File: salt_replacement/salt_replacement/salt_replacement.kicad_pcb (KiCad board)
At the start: 2 copper layers, 35 x 21 mm, 17 parts, among them J1 SALT chip package pins, Q1 FDG1024NZ, U1 IC REG BUCK SEPIC 5V 4.5A 8SO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, U2 MAX3232

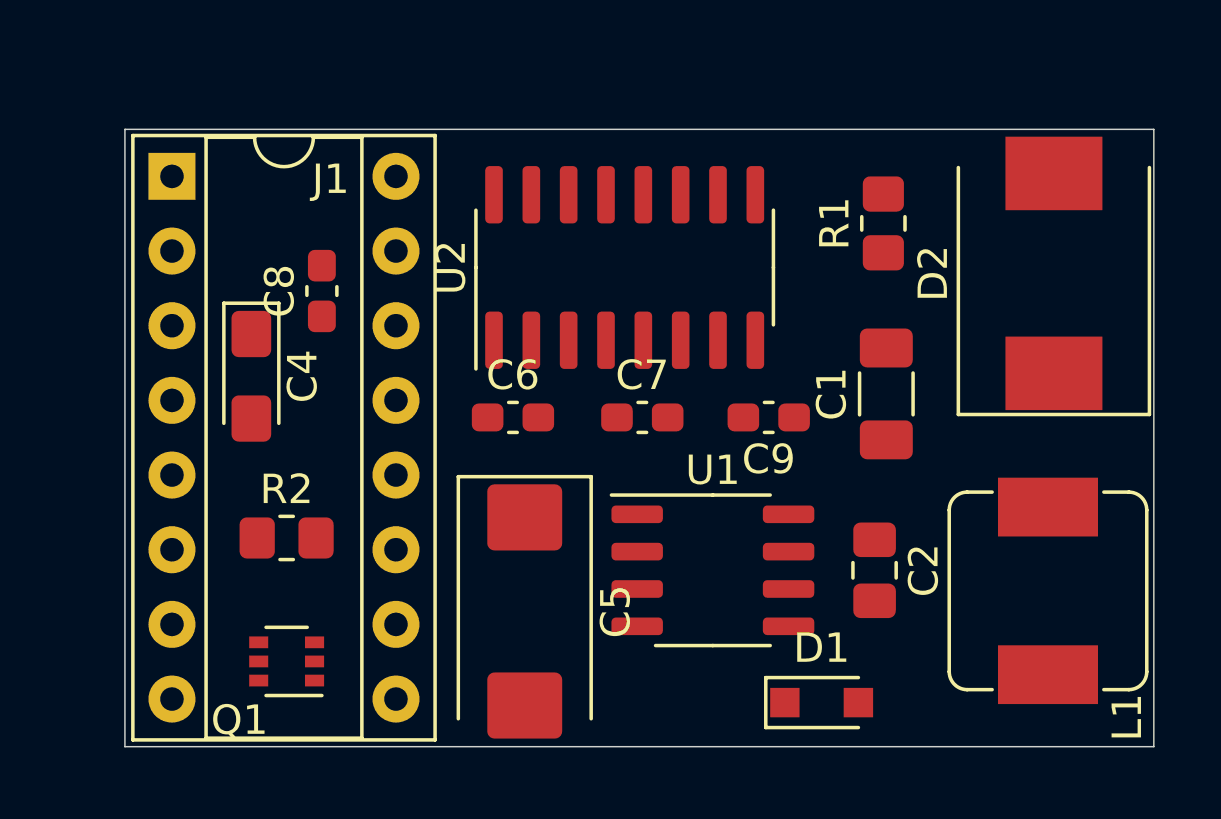
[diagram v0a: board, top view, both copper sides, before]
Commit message: -complete redesign -replaced all components with jclpcb stock -added non-inverting zero crossing circuit.
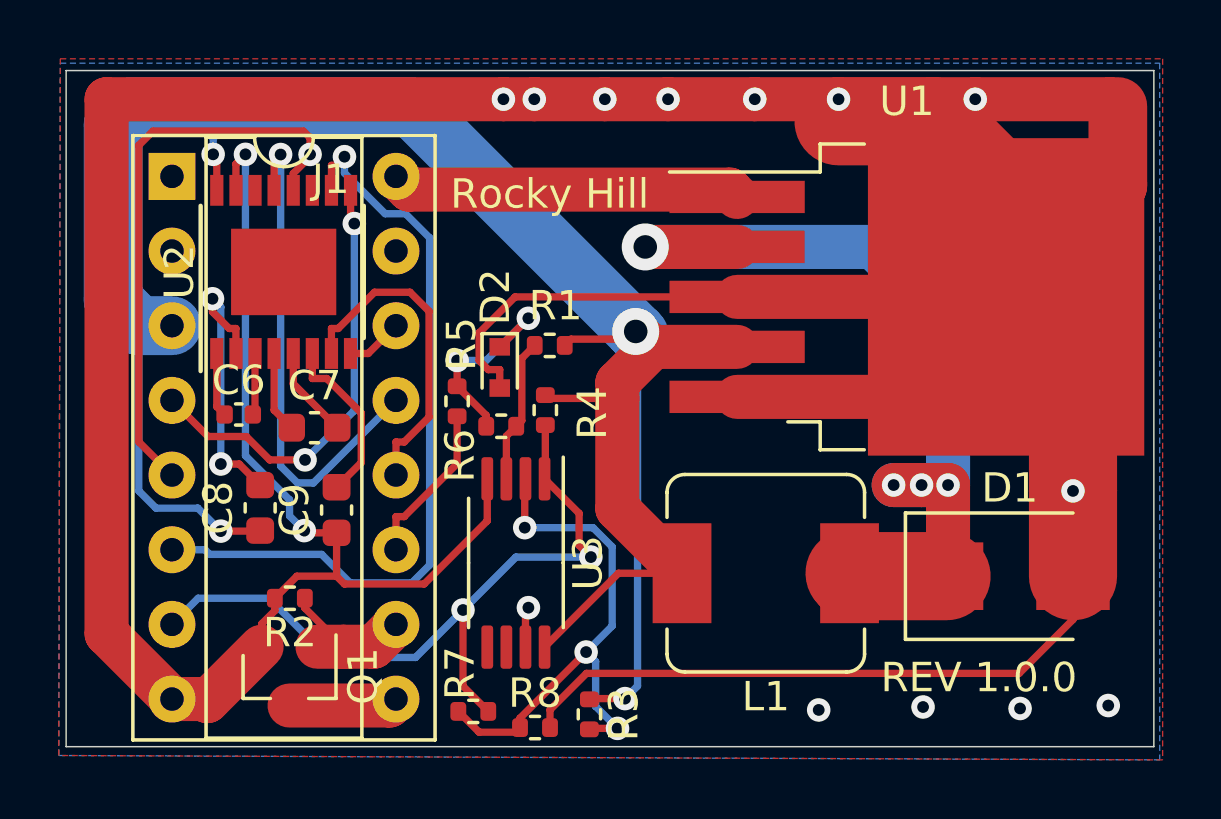
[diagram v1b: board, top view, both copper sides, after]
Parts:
- removed C1: .27uF, Capacitor_SMD:C_1206_3216Metric_Pad1.33x1.80mm_HandSolder
- removed C2: 5000pF, Capacitor_SMD:C_0805_2012Metric_Pad1.18x1.45mm_HandSolder
- removed C4: 10uF, Capacitor_Tantalum_SMD:CP_EIA-3216-18_Kemet-A_Pad1.58x1.35mm_HandSolder
- removed C5: 100uF, Capacitor_Tantalum_SMD:CP_EIA-7343-31_Kemet-D_Pad2.25x2.55mm_HandSolder
- added R3: 100K, Resistor_SMD:R_0402_1005Metric, F.Cu at (125.8, 129.9)
- added R4: 5.1K, Resistor_SMD:R_0402_1005Metric, F.Cu at (124.3, 119.5)
- added R5: 5.1K, Resistor_SMD:R_0402_1005Metric, F.Cu at (121.3, 119.2)
- added R6: 5.1K, Resistor_SMD:R_0402_1005Metric, F.Cu at (122.8, 120.1)
- added R7: 20M, Resistor_SMD:R_0402_1005Metric, F.Cu at (121.8, 129.8)
- added R8: 10K, Resistor_SMD:R_0402_1005Metric, F.Cu at (124.0, 130.3)
- added U3: LM393, Package_SO:TSSOP-8_4.4x3mm_P0.65mm, F.Cu at (123.3, 124.8)
- C6: footprint Capacitor_SMD:C_0603_1608Metric_Pad1.08x0.95mm_HandSolder -> Capacitor_SMD:C_0402_1005Metric
- C7, C8, C9: footprint Capacitor_SMD:C_0603_1608Metric_Pad1.08x0.95mm_HandSolder -> Capacitor_SMD:C_0603_1608Metric
- D1: value CMDSH-3 -> 5A 40V; footprint Diode_SMD:D_SOD-323_HandSoldering -> Diode_SMD:D_SMB
- D2: value B340LB-13-F -> 1N4148; footprint Diode_SMD:D_SMC -> Diode_SMD:D_SOD-523
- L1: value 10uH -> 33uH; footprint salt_replacement:L_Sumida_CDMC6D28_7.25x6.5mm -> Inductor_SMD:L_Sumida_CDMC6D28_7.25x6.5mm
- Q1: value FDG1024NZ -> MMBT9014C; footprint Package_TO_SOT_SMD:SOT-363_SC-70-6 -> Package_TO_SOT_SMD:SOT-23
- R1: value 10K -> 100K; footprint Resistor_SMD:R_0805_2012Metric_Pad1.20x1.40mm_HandSolder -> Resistor_SMD:R_0402_1005Metric
- R2: footprint Resistor_SMD:R_0805_2012Metric_Pad1.20x1.40mm_HandSolder -> Resistor_SMD:R_0402_1005Metric
- U1: value IC REG BUCK SEPIC 5V 4.5A 8SOIC -> LM2596S-5; footprint Package_SO:SO-8_3.9x4.9mm_P1.27mm -> Package_TO_SOT_SMD:TO-263-5_TabPin3
- U2: footprint Package_SO:SOIC-16_3.9x9.9mm_P1.27mm -> Package_SO:TSSOP-16-1EP_4.4x5mm_P0.65mm
- moved D2 19.1 mm to (122.8, 118.1), turned to 270 degrees
- moved C9 15.0 mm to (117.2, 123.0), turned to 90 degrees
- moved R1 12.1 mm to (124.5, 117.3), turned to 180 degrees
- moved U2 11.6 mm to (115.4, 114.8)
- moved U1 11.4 mm to (136.6, 115.7)
- moved C7 11.2 mm to (116.5, 120.2)
- moved L1 9.62 mm to (131.8, 125.1), turned to 180 degrees
- moved C6 9.33 mm to (113.9, 119.7)
- moved D1 7.71 mm to (140.1, 125.2)
- moved C8 7.67 mm to (114.6, 122.9)
- moved R2 2.05 mm to (115.6, 126.0), turned to 180 degrees
- moved Q1 0.51 mm to (115.6, 128.6), turned to 270 degrees
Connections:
- C8 pad 1: Net-(C8-Pad1) -> +5V
- C8 pad 2: +5V -> Net-(C8-Pad2)
- D1 pad 1: Net-(C1-Pad1) -> Net-(D1-Pad1)
- D1 pad 2: +5V -> GND
- D2 pad 1: Net-(C1-Pad2) -> Net-(D2-Pad1)
- J1 pad 11: Net-(J1-Pad11) -> /CASSETTE_DATA_IN
- J1 pad 7: Net-(J1-Pad7) -> /CASSETTE_DATA_IN_TTL
- L1 pad 1: Net-(C1-Pad2) -> Net-(D1-Pad1)
- Q1 pad 1: GND -> Net-(J1-Pad10)
- Q1 pad 2: Net-(J1-Pad10) -> GND
- Q1 pad 3: Net-(Q1-Pad3) -> Net-(J1-Pad9)
- R1 pad 1: Net-(C2-Pad1) -> +5V
- R1 pad 2: GND -> Net-(R1-Pad2)
- U1 pad 2: Net-(C1-Pad1) -> Net-(D1-Pad1)
- U1 pad 3: +5V -> GND
- U1 pad 4: GND -> +5V
- U1 pad 5: +5V -> GND
- U2 pad 2: Net-(C8-Pad1) -> Net-(C8-Pad2)
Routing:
- net GND: track 0.00 -> 170.3 mm, vias 0 -> 14
- net +5V: track 0.00 -> 81.0 mm, vias 0 -> 4
- net Net-(D1-Pad1): track 0.00 -> 30.2 mm, vias 0 -> 4
- net /SERIAL_OUT_TTL: track 0.00 -> 26.4 mm, vias 0 -> 1
- net /CASSETTE_DATA_IN_TTL: track 0.00 -> 25.8 mm, vias 0 -> 2
- net /CD_IN_TTL: track 0.00 -> 19.8 mm, vias 0 -> 1
- net Net-(R3-Pad2): track 0.00 -> 18.8 mm, vias 0 -> 3
- net /CD_IN_RS232: track 0.00 -> 17.2 mm, vias 0 -> 1
- net /SERIAL_IN_TTL: track 0.00 -> 15.3 mm, vias 0 -> 2
- net VCC: track 0.00 -> 11.9 mm
- net /SERIAL_OUT_RS232: track 0.00 -> 11.2 mm
- net Net-(C8-Pad2): track 0.00 -> 9.70 mm, vias 0 -> 2
- net Net-(D2-Pad1): track 0.00 -> 7.04 mm, vias 0 -> 2
- net Net-(C9-Pad2): track 0.00 -> 5.87 mm
- net /CASSETTE_DATA_IN: track 0.00 -> 5.57 mm
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- added copper zone on B.Cu, net GND
- added copper zone on F.Cu, net GND
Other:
- board size 35 x 21 mm -> 37 x 23 mm
- board text added: "REV 1.0.0"
- board text added: "Rocky Hill"
